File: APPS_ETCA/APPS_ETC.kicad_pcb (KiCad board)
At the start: 2 copper layers, 81.3 x 86.4 mm, 21 parts, among them P1 DTM1312PC12PDR008, U1 NUCLEO-L432KC, U2 MCP6004, U6 LM7805_TO220, U8 LM7809_TO220

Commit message: updated pcb
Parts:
- moved FS-2 APPS/ETC Board 9.27 mm to (236.9, 54.7)
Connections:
- R1 pad 1: Net-(U2A-+) -> Net-(U2A--)
- R3 pad 1: Net-(U2B-+) -> Net-(U2B--)
- R7 pad 1: Net-(U2C-+) -> Net-(U2C--)
- U2 pad 1: Net-(U2A-+) -> Net-(U2A--)
- U2 pad 10: Net-(U2C-+) -> /Brake Sensor
- U2 pad 2: /OUT1 -> Net-(U2A--)
- U2 pad 3: Net-(U2A-+) -> /OUT1
- U2 pad 5: Net-(U2B-+) -> /OUT2
- U2 pad 6: /OUT2 -> Net-(U2B--)
- U2 pad 7: Net-(U2B-+) -> Net-(U2B--)
- U2 pad 8: Net-(U2C-+) -> Net-(U2C--)
- U2 pad 9: /Brake Sensor -> Net-(U2C--)
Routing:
- net Net-(U2C-+): track 35.9 -> 0.00 mm, vias 1 -> 0
- net Net-(U2A-+): track 35.4 -> 0.00 mm
- net Net-(U2C--): track 0.00 -> 31.8 mm, vias 0 -> 1
- net Net-(U2A--): track 0.00 -> 27.6 mm
- net Net-(U2B-+): track 22.6 -> 0.00 mm
- net Net-(U2B--): track 0.00 -> 20.8 mm
- net /OUT2: track 77.7 -> 80.2 mm
- net /OUT1: track 91.1 -> 89.2 mm
- net /Brake Sensor: track 51.5 -> 53.3 mm
- net +5V: track 150.1 -> 151.7 mm
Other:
- board text added: "FS-2 APPS/ETC Board Formula Slug V 1.2 Creators: Abhi C. & Dustin W."
- board text removed: "FS-2 APPS/ETC Board Formula Slug V 1.1"

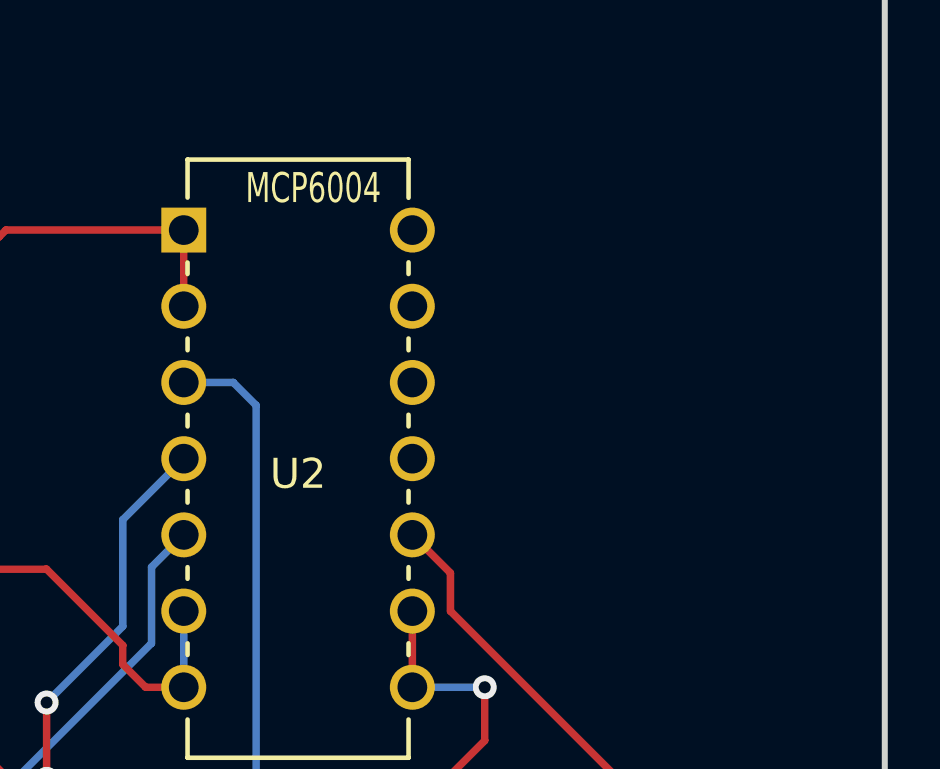
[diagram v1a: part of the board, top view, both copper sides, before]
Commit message: 100k Pull down resistor for all inputs to MCU pre- opamp
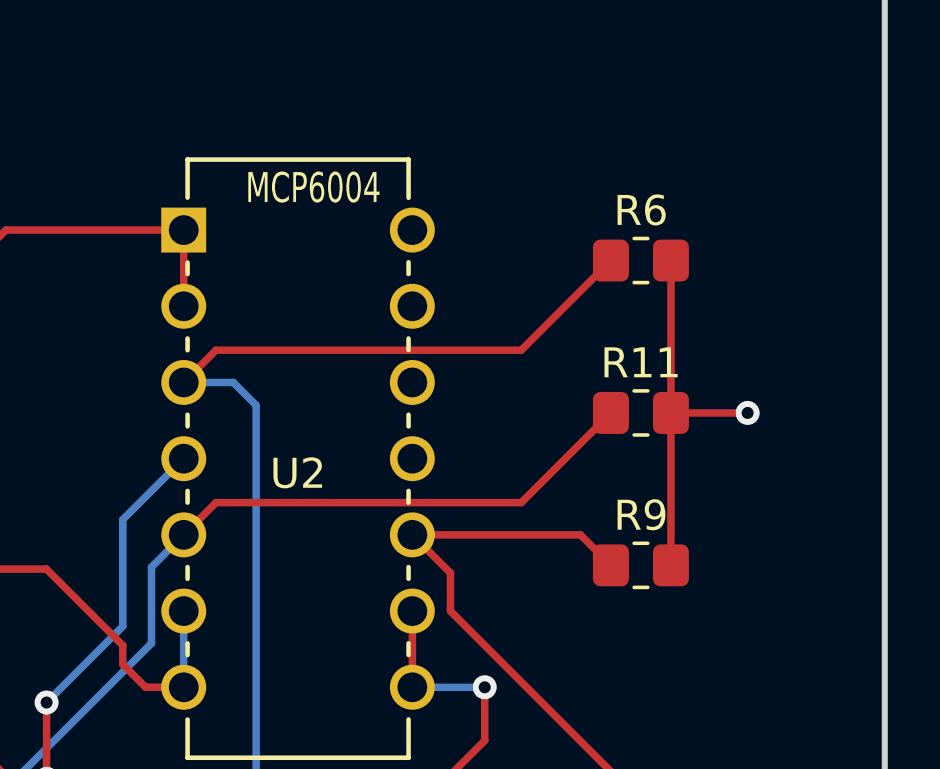
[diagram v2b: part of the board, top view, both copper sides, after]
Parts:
- added R11: 100k, Resistor_SMD:R_0805_2012Metric_Pad1.20x1.40mm_HandSolder, F.Cu at (243.3, 81.8)
- added R6: 100k, Resistor_SMD:R_0805_2012Metric_Pad1.20x1.40mm_HandSolder, F.Cu at (243.3, 76.7)
- added R9: 100k, Resistor_SMD:R_0805_2012Metric_Pad1.20x1.40mm_HandSolder, F.Cu at (243.3, 86.9)
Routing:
- net /OUT1: track 89.2 -> 105.1 mm
- net /OUT2: track 80.2 -> 96.1 mm
- net GND: track 70.6 -> 83.3 mm, vias 3 -> 4
- net /Brake Sensor: track 53.3 -> 60.3 mm

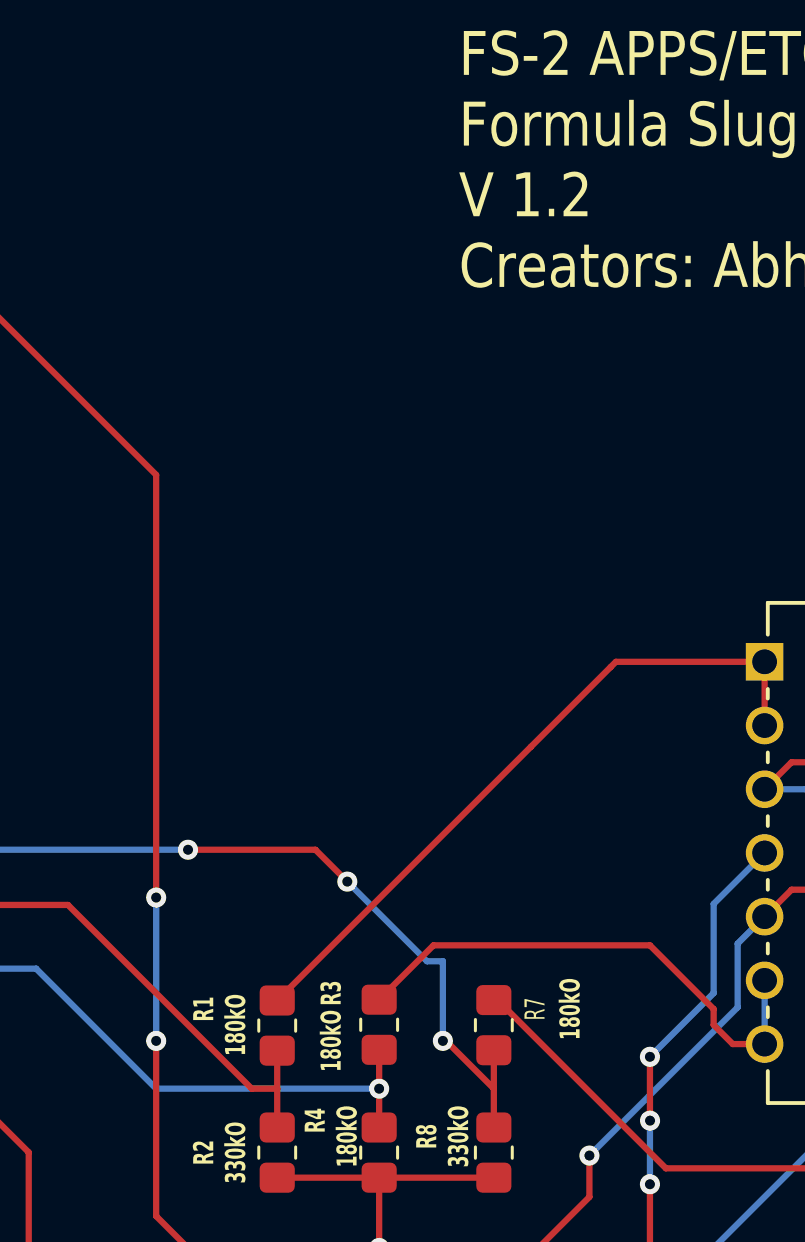
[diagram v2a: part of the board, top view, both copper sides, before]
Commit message: Add decoupling capacitor to analog inputs. 40 nF for 50 hz sample rate.
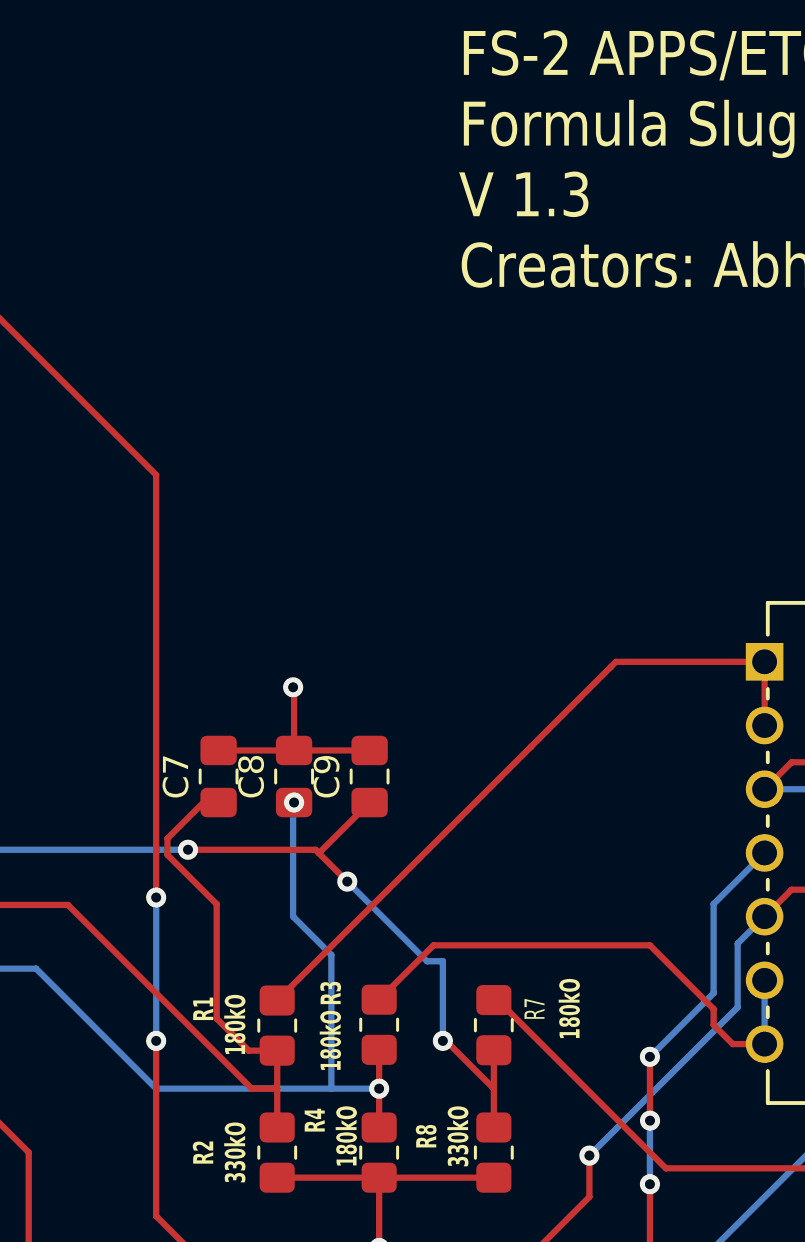
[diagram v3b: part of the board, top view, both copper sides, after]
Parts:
- added C7: 40 nF, Capacitor_SMD:C_0805_2012Metric_Pad1.18x1.45mm_HandSolder, F.Cu at (206.3, 80.3)
- added C8: 40 nF, Capacitor_SMD:C_0805_2012Metric_Pad1.18x1.45mm_HandSolder, F.Cu at (209.3, 80.3)
- added C9: 40 nF, Capacitor_SMD:C_0805_2012Metric_Pad1.18x1.45mm_HandSolder, F.Cu at (212.3, 80.3)
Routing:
- net /OUT1*: track 19.2 -> 32.7 mm
- net /OUT2*: track 22.2 -> 34.3 mm, vias 1 -> 2
- net GND: track 83.3 -> 91.8 mm, vias 4 -> 5
- net /Brake Sensor*: track 30.7 -> 33.6 mm
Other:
- board text added: "FS-2 APPS/ETC Board Formula Slug V 1.3 Creators: Abhi C. & Dustin W."
- board text removed: "FS-2 APPS/ETC Board Formula Slug V 1.2 Creators: Abhi C. & Dustin W."

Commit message: v1.3
this one for my boy COLE LEWI
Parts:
- C1: value 0.33 mF -> 0.33 uF
- C2, C6: value 0.1 mF -> 0.1 uF
- C5: value 0.33mF -> 0.33uF
- C7, C8: value 40 nF -> .047 uF
- C9: value 40 nF -> .047 uf
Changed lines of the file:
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@@
       (drillshape 0)
       (scaleselection 1)
-      (outputdirectory "/Users/abhinavchaubey/Desktop/APPS_ETC_v2/")
+      (outputdirectory "/Users/abhinavchaubey/Desktop/APPS_ETC_v3_GERBER/")
     )
   )
@@
     (fp_line (start 1 0.625) (end -1 0.625)
       (stroke (width 0.1) (type solid)) (layer "F.Fab"))
-    (pad "1" smd roundrect (at -1 0) (size 1.2 1.4) (layers "F.Cu" "F.Paste" "F.Mask") (roundrect_rratio 0.208333)
+    (pad "1" smd roundrect (at -1 0) (size 1.2 1.4) (layers "F.Cu" "F.Paste" "F.Mask") (roundrect_rratio 0.2083333333)
       (net 12 "/OUT2") (pintype "passive"))
-    (pad "2" smd roundrect (at 1 0) (size 1.2 1.4) (layers "F.Cu" "F.Paste" "F.Mask") (roundrect_rratio 0.208333)
+    (pad "2" smd roundrect (at 1 0) (size 1.2 1.4) (layers "F.Cu" "F.Paste" "F.Mask") (roundrect_rratio 0.2083333333)
       (net 2 "GND") (pintype "passive"))
     (model "${KICAD6_3DMODEL_DIR}/Resistor_SMD.3dshapes/R_0805_2012Metric.wrl"
@@
     (property "ki_keywords" "cap capacitor")
     (attr smd)
-    (fp_text reference "C9" (at 0 -1.68 90) (layer "F.SilkS")
-        (effects (font (size 1 1) (thickness 0.15)))
-    )
-    (fp_text value "40 nF" (at 0 1.68 90) (layer "F.Fab")
+    (fp_text reference "C9" (at 4.064 1.016 180) (layer "F.SilkS")
+        (effects (font (size 1 1) (thickness 0.15)))
+    )
+    (fp_text value ".047 uf" (at 2.794 1.016 180) (layer "F.Fab")
         (effects (font (size 1 1) (thickness 0.15)))
     )
@@
     (fp_line (start 1 0.625) (end -1 0.625)
       (stroke (width 0.1) (type solid)) (layer "F.Fab"))
-    (pad "1" smd roundrect (at -1.0375 0 90) (size 1.175 1.45) (layers "F.Cu" "F.Paste" "F.Mask") (roundrect_rratio 0.212766)
+    (pad "1" smd roundrect (at -1.0375 0 90) (size 1.175 1.45) (layers "F.Cu" "F.Paste" "F.Mask") (roundrect_rratio 0.2127659574)
       (net 30 "/Brake Sensor*") (pintype "passive"))
-    (pad "2" smd roundrect (at 1.0375 0 90) (size 1.175 1.45) (layers "F.Cu" "F.Paste" "F.Mask") (roundrect_rratio 0.212766)
+    (pad "2" smd roundrect (at 1.0375 0 90) (size 1.175 1.45) (layers "F.Cu" "F.Paste" "F.Mask") (roundrect_rratio 0.2127659574)
       (net 2 "GND") (pintype "passive"))
     (model "${KICAD6_3DMODEL_DIR}/Capacitor_SMD.3dshapes/C_0805_2012Metric.wrl"
@@
         (effects (font (size 0.8 0.5) (thickness 0.1) bold))
     )
-    (fp_text value "0.1 mF" (at 0.0215 -2.032) (layer "F.SilkS")
+    (fp_text value "0.1 uF" (at 0.0215 -2.032) (layer "F.SilkS")
         (effects (font (size 0.8 0.5) (thickness 0.1) bold))
     )
@@
     (property "ki_keywords" "cap capacitor")
     (attr smd)
-    (fp_text reference "C7" (at 0 -1.68 90) (layer "F.SilkS")
-        (effects (font (size 1 1) (thickness 0.15)))
-    )
-    (fp_text value "40 nF" (at 0 1.68 90) (layer "F.Fab")
+    (fp_text reference "C7" (at 4.064 -0.584 180) (layer "F.SilkS")
+        (effects (font (size 1 1) (thickness 0.15)))
+    )
+    (fp_text value ".047 uF" (at 2.794 -0.584 180) (layer "F.Fab")
         (effects (font (size 1 1) (thickness 0.15)))
     )
@@
     (fp_line (start 1 0.625) (end -1 0.625)
       (stroke (width 0.1) (type solid)) (layer "F.Fab"))
-    (pad "1" smd roundrect (at -1.0375 0 90) (size 1.175 1.45) (layers "F.Cu" "F.Paste" "F.Mask") (roundrect_rratio 0.212766)
+    (pad "1" smd roundrect (at -1.0375 0 90) (size 1.175 1.45) (layers "F.Cu" "F.Paste" "F.Mask") (roundrect_rratio 0.2127659574)
       (net 17 "/OUT1*") (pintype "passive"))
-    (pad "2" smd roundrect (at 1.0375 0 90) (size 1.175 1.45) (layers "F.Cu" "F.Paste" "F.Mask") (roundrect_rratio 0.212766)
+    (pad "2" smd roundrect (at 1.0375 0 90) (size 1.175 1.45) (layers "F.Cu" "F.Paste" "F.Mask") (roundrect_rratio 0.2127659574)
       (net 2 "GND") (pintype "passive"))
     (model "${KICAD6_3DMODEL_DIR}/Capacitor_SMD.3dshapes/C_0805_2012Metric.wrl"
@@
         (effects (font (size 0.8 0.5) (thickness 0.1) bold))
     )
-    (fp_text value "0.1 mF" (at -0.1485 -2.032) (layer "F.SilkS")
+    (fp_text value "0.1 uF" (at -0.1485 -2.032) (layer "F.SilkS")
         (effects (font (size 0.8 0.5) (thickness 0.1) bold))
     )
@@
     (property "ki_keywords" "cap capacitor")
     (attr smd)
-    (fp_text reference "C8" (at 0 -1.68 90) (layer "F.SilkS")
-        (effects (font (size 1 1) (thickness 0.15)))
-    )
-    (fp_text value "40 nF" (at 0 1.68 90) (layer "F.Fab")
+    (fp_text reference "C8" (at 6.604 0.216 180) (layer "F.SilkS")
+        (effects (font (size 1 1) (thickness 0.15)))
+    )
+    (fp_text value ".047 uF" (at 5.334 0.216 180) (layer "F.Fab")
         (effects (font (size 1 1) (thickness 0.15)))
     )
@@
     (fp_line (start 1 0.625) (end -1 0.625)
       (stroke (width 0.1) (type solid)) (layer "F.Fab"))
-    (pad "1" smd roundrect (at -1.0375 0 90) (size 1.175 1.45) (layers "F.Cu" "F.Paste" "F.Mask") (roundrect_rratio 0.212766)
+    (pad "1" smd roundrect (at -1.0375 0 90) (size 1.175 1.45) (layers "F.Cu" "F.Paste" "F.Mask") (roundrect_rratio 0.2127659574)
       (net 28 "/OUT2*") (pintype "passive"))
-    (pad "2" smd roundrect (at 1.0375 0 90) (size 1.175 1.45) (layers "F.Cu" "F.Paste" "F.Mask") (roundrect_rratio 0.212766)
+    (pad "2" smd roundrect (at 1.0375 0 90) (size 1.175 1.45) (layers "F.Cu" "F.Paste" "F.Mask") (roundrect_rratio 0.2127659574)
       (net 2 "GND") (pintype "passive"))
     (model "${KICAD6_3DMODEL_DIR}/Capacitor_SMD.3dshapes/C_0805_2012Metric.wrl"
@@
         (effects (font (size 0.8 0.5) (thickness 0.1) bold))
     )
-    (fp_text value "0.33 mF" (at 0 2.032) (layer "F.SilkS")
+    (fp_text value "0.33 uF" (at 0 2.032) (layer "F.SilkS")
         (effects (font (size 0.8 0.5) (thickness 0.1) bold))
     )
@@
     (fp_line (start 1 0.625) (end -1 0.625)
       (stroke (width 0.1) (type solid)) (layer "F.Fab"))
-    (pad "1" smd roundrect (at -1 0) (size 1.2 1.4) (layers "F.Cu" "F.Paste" "F.Mask") (roundrect_rratio 0.208333)
+    (pad "1" smd roundrect (at -1 0) (size 1.2 1.4) (layers "F.Cu" "F.Paste" "F.Mask") (roundrect_rratio 0.2083333333)
       (net 14 "/Brake Sensor") (pintype "passive"))
-    (pad "2" smd roundrect (at 1 0) (size 1.2 1.4) (layers "F.Cu" "F.Paste" "F.Mask") (roundrect_rratio 0.208333)
+    (pad "2" smd roundrect (at 1 0) (size 1.2 1.4) (layers "F.Cu" "F.Paste" "F.Mask") (roundrect_rratio 0.2083333333)
       (net 2 "GND") (pintype "passive"))
     (model "${KICAD6_3DMODEL_DIR}/Resistor_SMD.3dshapes/R_0805_2012Metric.wrl"
@@
         (effects (font (size 0.8 0.5) (thickness 0.1) bold))
     )
-    (fp_text value "0.33mF" (at 0.1485 2.032) (layer "F.SilkS")
+    (fp_text value "0.33uF" (at 0.1485 2.032) (layer "F.SilkS")
         (effects (font (size 0.8 0.5) (thickness 0.1) bold))
     )
@@
     (fp_line (start 1 0.625) (end -1 0.625)
       (stroke (width 0.1) (type solid)) (layer "F.Fab"))
-    (pad "1" smd roundrect (at -1 0) (size 1.2 1.4) (layers "F.Cu" "F.Paste" "F.Mask") (roundrect_rratio 0.208333)
+    (pad "1" smd roundrect (at -1 0) (size 1.2 1.4) (layers "F.Cu" "F.Paste" "F.Mask") (roundrect_rratio 0.2083333333)
       (net 13 "/OUT1") (pintype "passive"))
-    (pad "2" smd roundrect (at 1 0) (size 1.2 1.4) (layers "F.Cu" "F.Paste" "F.Mask") (roundrect_rratio 0.208333)
+    (pad "2" smd roundrect (at 1 0) (size 1.2 1.4) (layers "F.Cu" "F.Paste" "F.Mask") (roundrect_rratio 0.2083333333)
       (net 2 "GND") (pintype "passive"))
     (model "${KICAD6_3DMODEL_DIR}/Resistor_SMD.3dshapes/R_0805_2012Metric.wrl"
